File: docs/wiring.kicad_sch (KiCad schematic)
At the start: 9 parts, among them J1 M12 Socket, J16 TowerLight, J18 Barrel Jack, J2 M12 Pin, J3 M12 Socket, J4 M12 Socket, J5 M12 Socket, K1 Phoenix 2908215, K2 Relay_SPDT

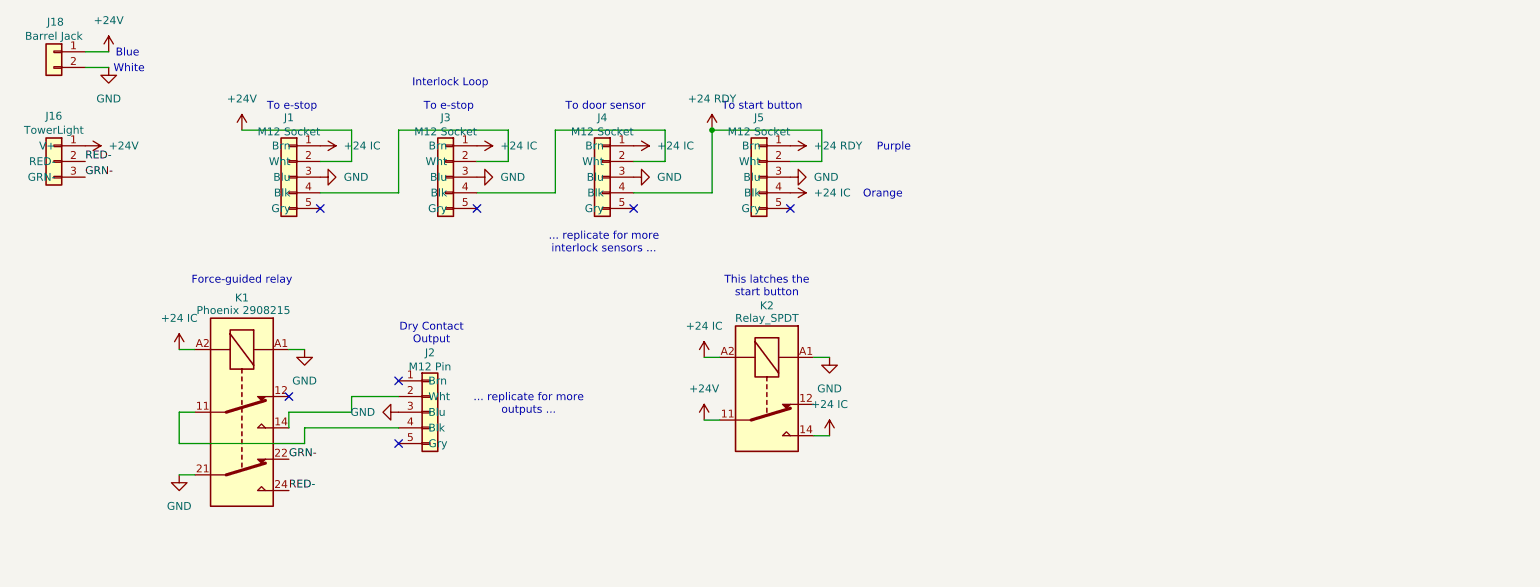
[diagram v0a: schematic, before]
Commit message: Update wiring diagram with equipment-off based indicator and mismatch detect
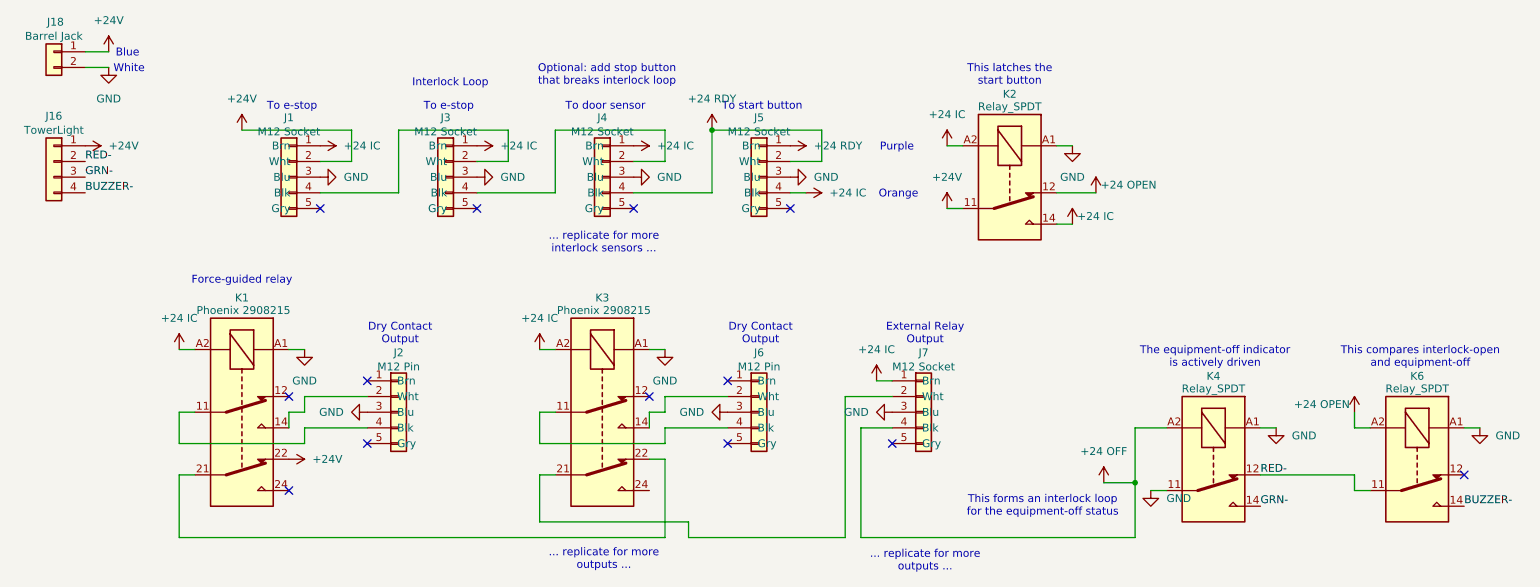
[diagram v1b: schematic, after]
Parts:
- added J6: M12 Pin, symbol Connector_Generic:Conn_01x05
- added J7: M12 Socket, symbol Connector_Generic:Conn_01x05
- added K3: Phoenix 2908215, symbol Relay:Relay_DPDT
- added K4, K6: Relay_SPDT, symbol Relay:Relay_SPDT
- J16: symbol Connector_Generic:Conn_01x03 -> Connector_Generic:Conn_01x04
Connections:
- net +24 IC: now also J7.1 (Brn), K3.A2
- net +24V: now also K1.22
- net GND: now also J6.3 (Blu), J7.3 (Blu), K3.A1, K4.11, K4.A1, K6.A1; no longer K1.21
- net GRN-: now also K4.14; no longer K1.22
- net RED-: now also K4.12, K6.11; no longer K1.24
- net +24 OPEN: now reaches K2.12
- net +24 OPEN: now also K6.A2
- new net: J6.4 (Blk), K3.11
- new net: J6.2 (Wht), K3.14
- new net: J7.2 (Wht), K3.21
- new net: K1.21, K3.22
- new net +24 OFF: J7.4 (Blk), K4.A2
- new net BUZZER-: J16.4 (Pin_4), K6.14
- no-connect marks 7 -> 13
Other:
- note added: "External Relay Output"
- note added: "Optional: add stop button that breaks interlock loop"
- note added: "The equipment-off indicator is actively driven"
- note added: "This compares interlock-open and equipment-off"
- note added: "This forms an interlock loop for the equipment-off status"
- moved on the sheet: J16, J2, K2
